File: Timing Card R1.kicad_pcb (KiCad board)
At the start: 4 copper layers, 65 x 41.6 mm, 140 parts, among them J1 71430-0101, J10 10018784-10201TLF, J2 Conn_01x10, U1 LCMXO2-7000HC-6TG144I, U10 74AHC125, U11 T602-025.0M, U12 FM24C64B, U2 SN74LVC1G125DRL, U3 74AHCT125, U4 74AHCT125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

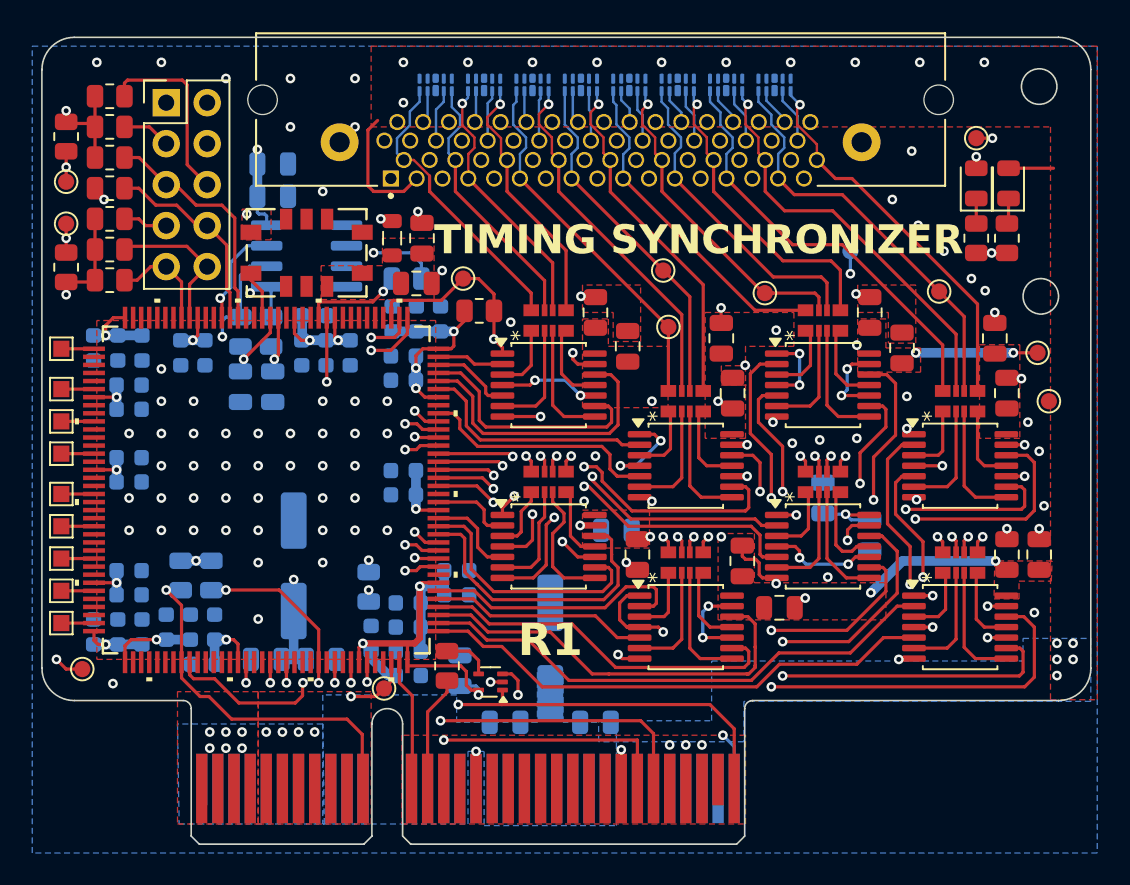
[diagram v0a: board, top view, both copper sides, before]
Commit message: Updated libraries
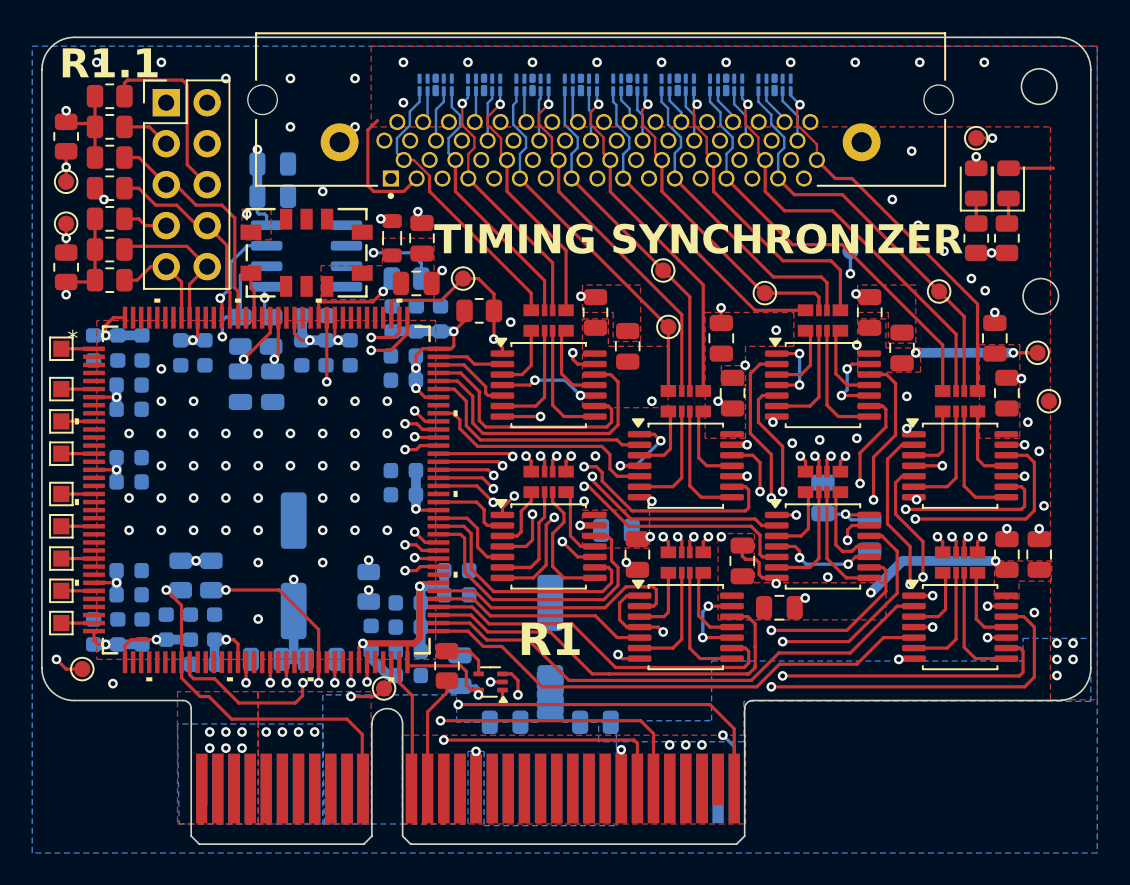
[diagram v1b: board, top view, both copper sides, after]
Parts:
- J1: footprint Connector:MOLEX_71430-0101 -> Footprints:MOLEX_71430-0101
- R15, R16, R17, R18, R20, R21, R22, R23: footprint Resistor_SMD:EXB28V_PAN -> Footprints:EXB28V_PAN
- U1: footprint Package_QFP:TQFP144_LAT -> Footprints:TQFP144_LAT
- U11: footprint Oscillator:T602-025.0M_CNW -> Footprints:T602-025.0M_CNW
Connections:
- U1 pad 127: /FPGA/OSC_OUT -> unconnected-(U1B-PT18B-Pad127)
- U1 pad 128: unconnected-(U1B-PT18A-Pad128) -> /FPGA/OSC_OUT
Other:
- board text added: "R1.1"
